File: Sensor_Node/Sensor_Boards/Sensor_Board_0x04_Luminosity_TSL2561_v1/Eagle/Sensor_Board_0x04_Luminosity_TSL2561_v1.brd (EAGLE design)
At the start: 55 x 35 mm, 16 parts, among them J1 M04_SMD_90, J4 ARDUINO_ISP, U2 ATMEGA328P_TQFP, Y1 8MHZ

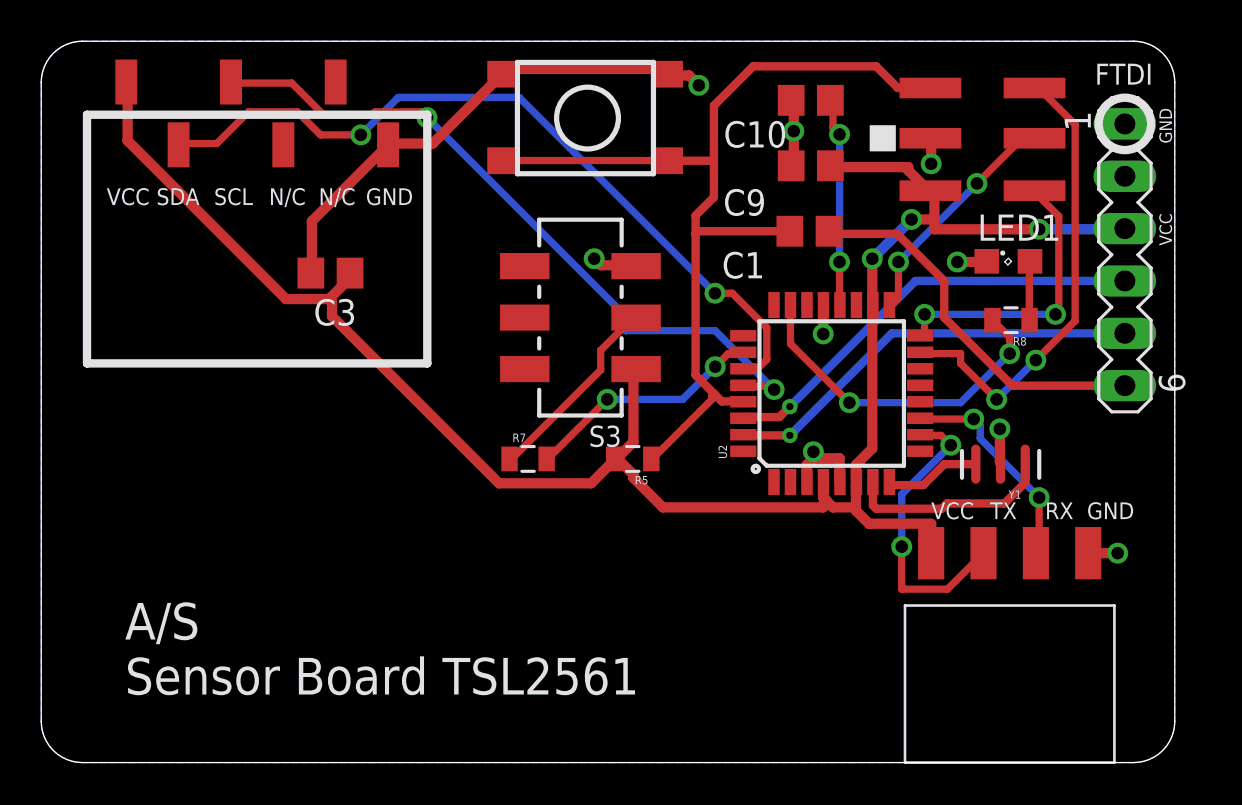
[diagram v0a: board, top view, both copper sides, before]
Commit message: Update SensorBoard TSL2561
new reference print - updated all placements, defined positions of
connectors and improved routing.
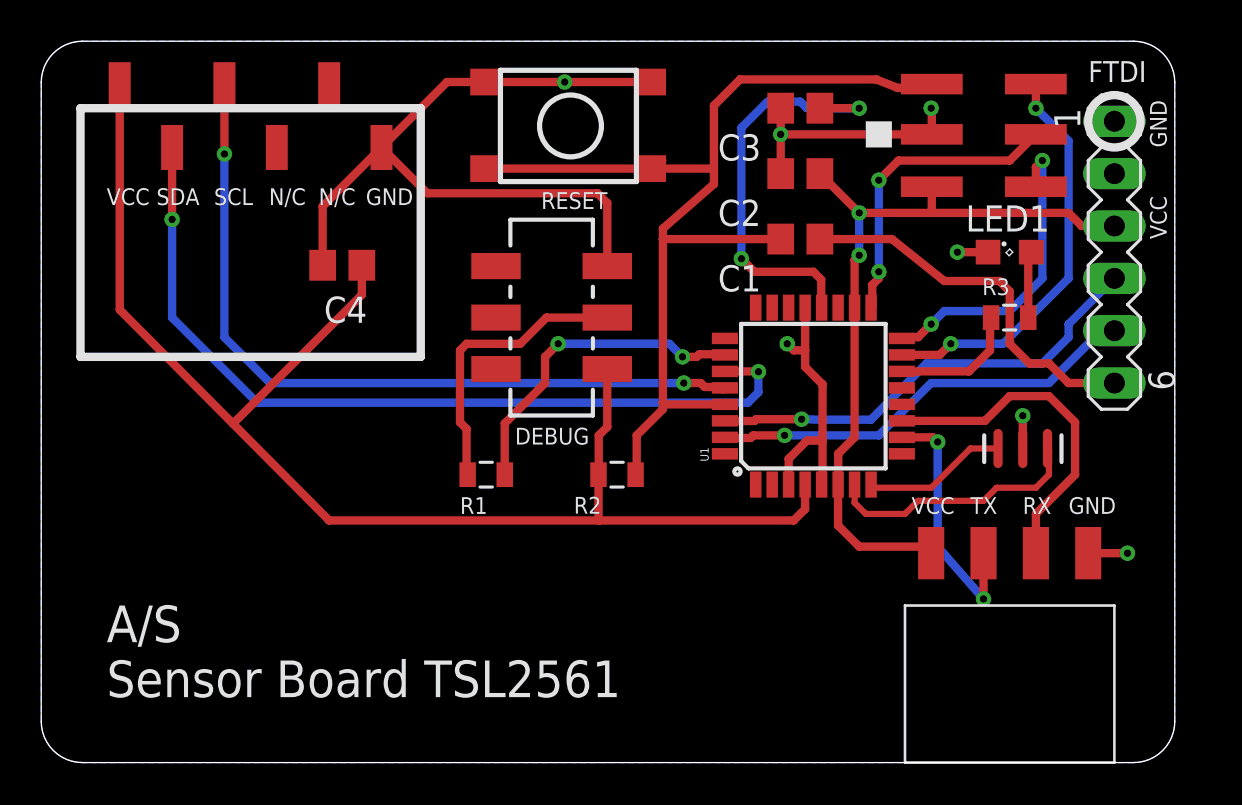
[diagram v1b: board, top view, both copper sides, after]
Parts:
- removed C10, C9: 100n, eagle-ltspice:C0805
- removed R5, R7: 10k, SparkFun-Passives:0805
- removed R8: 330, SparkFun-Passives:0805
- removed S3: JS202011SCQN, myownthings:JS202011SCQN
- removed U$9: M06_SMD_STRAIGHT, wsn:M06_SMD_STRAIGHT
- removed U2: ATMEGA328P_TQFP, marc_library:TQFP32-08
- added C2, C4: 100n, eagle-ltspice:C0805
- added R1, R2: 10k, SparkFun-Passives:0805
- added R3: 330, SparkFun-Passives:0805
- added S2: JS202011SCQN, myownthings:JS202011SCQN
- added SV2: (no value), con-lstb:MA06-1
- added U1: ATMEGA328P_TQFP, marc_library:TQFP32-08
- SV1: value (none) -> M06_SMD_STRAIGHT; device con-lstb:MA06-1 -> wsn:M06_SMD_STRAIGHT
- moved SV1 36.4 mm to (16.5, 29.8), turned to 180 degrees
- moved C3 24.2 mm to (36.8, 31.8)
- moved Y1 1.32 mm to (47.6, 15.2)
- moved S1 0.91 mm to (21.6, 33.0)
- moved C1 0.59 mm to (36.8, 25.4)
- moved LED1 0.45 mm to (47.0, 24.8)
- moved J4 0.20 mm to (48.3, 27.9)
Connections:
- net DBG_ENABLE: now also R1.2, U1.26; no longer R7.2, U2.26
- net FTDI_RESET: now also SV2.6; no longer SV1.6
- net FTDI_RXI: now also SV2.4, U1.30; no longer SV1.4, U2.30
- net FTDI_TXO: now also SV2.5, U1.31; no longer SV1.5, U2.31
- net GND: now also C2.2, C4.2, S2.3, SV1.P1, SV2.1, SV2.2, U1.21, U1.3, U1.5; no longer C10.2, C9.2, S3.3, SV1.1, SV1.2, U$9.P1, U2.21, U2.3, U2.5
- net L1: now also R3.2, U1.14; no longer R8.2, U2.23
- net MCU_RXI: now also U1.11; no longer U2.11
- net MCU_TXO: now also U1.10; no longer U2.10
- net MISO: now also U1.16; no longer U2.16
- net MOSI: now also U1.15; no longer U2.15
- net N$1: now also U1.8; no longer U2.8
- net N$15: now also C3.1, U1.20; no longer C10.1, U2.20
- net N$2: now also U1.7; no longer U2.7
- net N$3: now also R1.1, S2.2; no longer R7.1, S3.2
- net N$30: now also R3.1; no longer R8.1
- net RESET: now also R2.1, U1.29; no longer R5.1, U2.29
- net SCK: now also U1.17; no longer U2.17
- net SCL: now also SV1.P4, U1.28; no longer U$9.P4, U2.28
- net SDA: now also SV1.P5, U1.27; no longer U$9.P5, U2.27
- net VCC: now also C2.1, C4.1, R2.2, S2.1, SV1.P6, SV2.3, U1.18, U1.4, U1.6; no longer C3.1, C9.1, R5.2, S3.1, SV1.3, U$9.P6, U2.18, U2.4, U2.6
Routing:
- net GND: track 41.6 -> 66.4 mm, vias 9 -> 7
- net VCC: track 93.4 -> 104.9 mm, vias 3 -> 2
- net L1: track 16.7 -> 6.31 mm, vias 2 -> 0
- net N$15: track 10.1 -> 20.3 mm
- net MCU_RXI: track 10.7 -> 16.6 mm, vias 2 -> 0
- net N$3: track 9.53 -> 14.0 mm
- net DBG_ENABLE: track 11.7 -> 15.8 mm
- net RESET: track 47.4 -> 51.3 mm
- net SCK: track 11.4 -> 14.9 mm
- net SDA: track 37.9 -> 41.2 mm
- net MOSI: track 22.7 -> 19.7 mm
- net SCL: track 34.8 -> 37.7 mm
- net N$2: track 10.0 -> 12.6 mm
- net N$1: track 4.68 -> 7.01 mm
- net MCU_TXO: track 14.4 -> 12.5 mm
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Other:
- board text added: "DEBUG"
- board text added: "RESET"

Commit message: Finished Changes on PulseBoard
Pulseboard:
- tidied up routing and placement

TSL2561:
- tidied up some connections
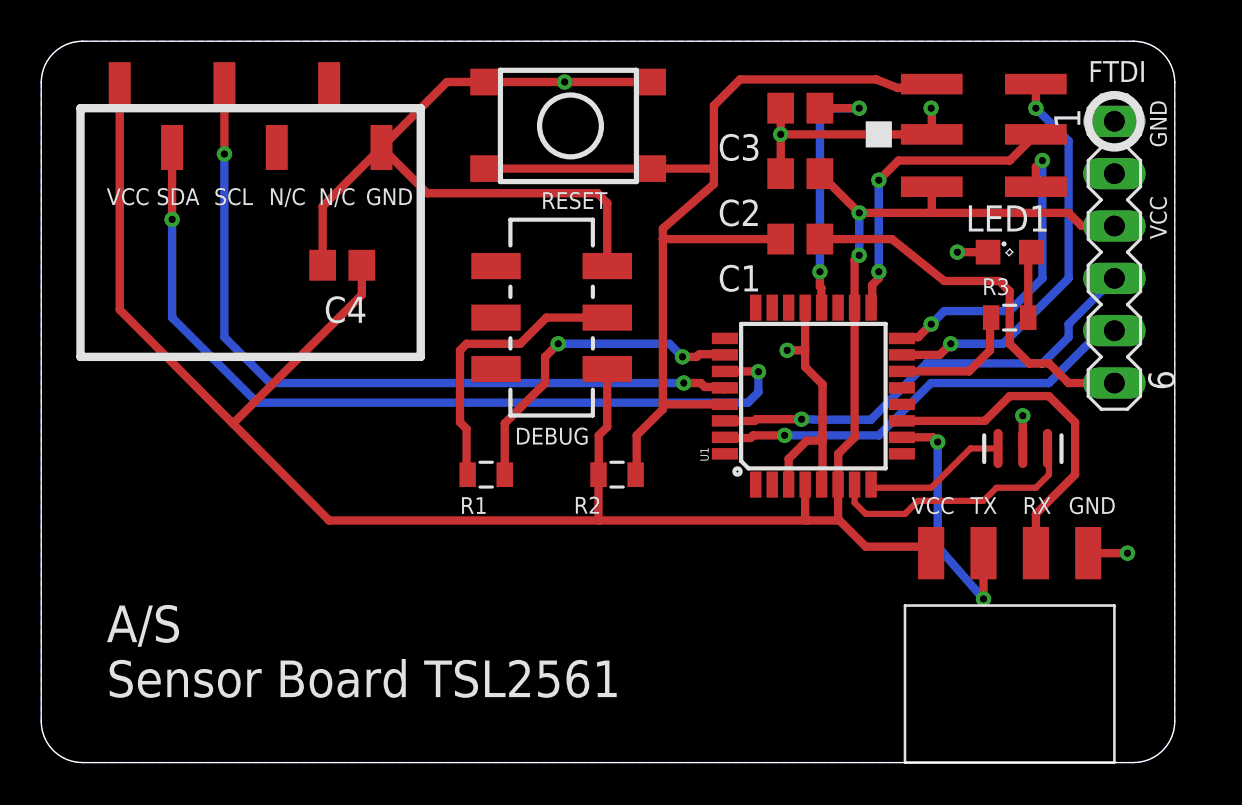
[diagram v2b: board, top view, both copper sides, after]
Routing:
- net N$15: track 20.3 -> 13.2 mm
- net VCC: track 104.9 -> 106.8 mm
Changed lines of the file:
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@@
 <?xml version="1.0" encoding="utf-8"?>
 <!DOCTYPE eagle SYSTEM "eagle.dtd">
-<eagle version="8.2.2">
+<eagle version="8.4.1">
 <drawing>
 <settings>
 <setting alwaysvectorfont="no"/>
+<setting keepoldvectorfont="yes"/>
 <setting verticaltext="up"/>
 </settings>
@@
 <param name="dpMaxLengthDifference" value="10mm"/>
 <param name="dpGapFactor" value="2.5"/>
-<param name="checkGrid" value="0"/>
 <param name="checkAngle" value="0"/>
 <param name="checkFont" value="1"/>
 <param name="checkRestrict" value="1"/>
+<param name="checkStop" value="0"/>
 <param name="useDiameter" value="13"/>
 <param name="maxErrors" value="50"/>
@@
 <wire x1="37.89541875" y1="15.621" x2="37.9095" y2="15.63508125" width="0.4064" layer="1"/>
 <via x="35.8775" y="30.48" extent="1-16" drill="0.35"/>
-<via x="36.195" y="20.32" extent="1-16" drill="0.35"/>
-<wire x1="37.065" y1="20.0025" x2="36.5125" y2="20.0025" width="0.4064" layer="1"/>
-<wire x1="36.5125" y1="20.0025" x2="36.195" y2="20.32" width="0.4064" layer="1"/>
+<via x="36.195" y="20.0025" extent="1-16" drill="0.35"/>
+<wire x1="37.065" y1="20.0025" x2="36.195" y2="20.0025" width="0.4064" layer="1"/>
 <via x="52.705" y="10.16" extent="1-16" drill="0.35"/>
 <wire x1="50.8" y1="10.16" x2="52.705" y2="10.16" width="0.4064" layer="1"/>
@@
 <wire x1="9.3053375" y1="16.441315625" x2="3.81" y2="21.971" width="0.4064" layer="1"/>
 <wire x1="9.3053375" y1="16.441315625" x2="13.97" y2="11.7475" width="0.4064" layer="1"/>
-<wire x1="37.065" y1="13.4874" x2="37.065" y2="12.3" width="0.4064" layer="1"/>
-<wire x1="37.065" y1="12.3" x2="36.5125" y2="11.7475" width="0.4064" layer="1"/>
-<wire x1="27.07931875" y1="11.7475" x2="36.5125" y2="11.7475" width="0.4064" layer="1"/>
-<wire x1="27.07931875" y1="11.7475" x2="13.97" y2="11.7475" width="0.4064" layer="1"/>
+<wire x1="13.97" y1="11.7475" x2="27.07931875" y2="11.7475" width="0.4064" layer="1"/>
 <wire x1="27.04" y1="13.97" x2="27.04" y2="11.78681875" width="0.4064" layer="1"/>
 <wire x1="27.04" y1="11.78681875" x2="27.07931875" y2="11.7475" width="0.4064" layer="1"/>
 <wire x1="15.555" y1="24.13" x2="15.555" y2="22.690978125" width="0.4064" layer="1"/>
 <wire x1="15.555" y1="22.690978125" x2="9.3053375" y2="16.441315625" width="0.4064" layer="1"/>
-<wire x1="38.665" y1="13.4874" x2="38.665" y2="11.5" width="0.4064" layer="1"/>
-<wire x1="38.665" y1="11.5" x2="39.6875" y2="10.4775" width="0.4064" layer="1"/>
-<wire x1="39.6875" y1="10.4775" x2="42.8625" y2="10.4775" width="0.4064" layer="1"/>
+<wire x1="38.665" y1="11.8175" x2="38.665" y2="13.4874" width="0.4064" layer="1"/>
+<wire x1="38.665" y1="11.7475" x2="38.665" y2="11.8175" width="0.4064" layer="1"/>
+<wire x1="38.665" y1="11.8175" x2="40.005" y2="10.4775" width="0.4064" layer="1"/>
+<wire x1="40.005" y1="10.4775" x2="42.8625" y2="10.4775" width="0.4064" layer="1"/>
 <wire x1="42.8625" y1="10.4775" x2="43.18" y2="10.16" width="0.4064" layer="1"/>
 <wire x1="39.465" y1="15.7795" x2="39.465" y2="22.0726" width="0.4064" layer="1"/>
@@
 <wire x1="49.8475" y1="26.67" x2="50.4825" y2="26.035" width="0.4064" layer="1"/>
 <wire x1="50.4825" y1="26.035" x2="52.07" y2="26.035" width="0.4064" layer="1"/>
-<wire x1="37.065" y1="13.4874" x2="38.6715" y2="13.4939" width="0" layer="19" extent="1-1"/>
+<wire x1="37.1475" y1="11.7475" x2="27.07931875" y2="11.7475" width="0.4064" layer="1"/>
+<wire x1="37.1475" y1="11.7475" x2="38.665" y2="11.7475" width="0.4064" layer="1"/>
+<wire x1="37.065" y1="11.83" x2="37.1475" y2="11.7475" width="0.4064" layer="1"/>
+<wire x1="37.065" y1="13.4874" x2="37.065" y2="11.83" width="0.4064" layer="1"/>
 </signal>
 <signal name="RESET">
@@
 <contactref element="C3" pad="1"/>
 <contactref element="U1" pad="20"/>
+<wire x1="37.78" y1="31.75" x2="39.6875" y2="31.75" width="0.4064" layer="1"/>
 <via x="39.6875" y="31.75" extent="1-16" drill="0.35"/>
-<wire x1="37.78" y1="31.75" x2="39.6875" y2="31.75" width="0.4064" layer="1"/>
-<wire x1="39.6875" y1="31.75" x2="37.1475" y2="31.75" width="0.4064" layer="16"/>
-<wire x1="37.1475" y1="31.75" x2="36.83" y2="32.0675" width="0.4064" layer="16"/>
-<wire x1="36.83" y1="32.0675" x2="35.2425" y2="32.0675" width="0.4064" layer="16"/>
-<wire x1="35.2425" y1="32.0675" x2="33.9725" y2="30.7975" width="0.4064" layer="16"/>
-<wire x1="33.9725" y1="30.7975" x2="33.9725" y2="24.4475" width="0.4064" layer="16"/>
-<via x="33.9725" y="24.4475" extent="1-16" drill="0.35"/>
-<wire x1="33.9725" y1="24.4475" x2="34.6075" y2="23.8125" width="0.4064" layer="1"/>
-<wire x1="34.6075" y1="23.8125" x2="37.465" y2="23.8125" width="0.4064" layer="1"/>
-<wire x1="37.465" y1="23.8125" x2="37.846" y2="23.4315" width="0.4064" layer="1"/>
-<wire x1="37.846" y1="23.4315" x2="37.846" y2="22.0916" width="0.4064" layer="1"/>
-<wire x1="37.846" y1="22.0916" x2="37.865" y2="22.0726" width="0.4064" layer="1"/>
+<wire x1="39.6875" y1="31.75" x2="38.4175" y2="31.75" width="0.4064" layer="16"/>
+<wire x1="38.4175" y1="31.75" x2="37.7825" y2="31.115" width="0.4064" layer="16"/>
+<wire x1="37.7825" y1="31.115" x2="37.7825" y2="23.8125" width="0.4064" layer="16"/>
+<via x="37.7825" y="23.8125" extent="1-16" drill="0.35"/>
+<wire x1="37.7825" y1="23.8125" x2="37.7825" y2="23.08821875" width="0.4064" layer="1"/>
+<wire x1="37.7825" y1="23.08821875" x2="37.85275625" y2="23.0179625" width="0.4064" layer="1"/>
+<wire x1="37.85275625" y1="23.0179625" x2="37.85275625" y2="22.08484375" width="0.4064" layer="1"/>
+<wire x1="37.85275625" y1="22.08484375" x2="37.865" y2="22.0726" width="0.4064" layer="1"/>
 </signal>
 <signal name="N$3">
@@
 </note>
 <note version="8.2" severity="warning">
-Since Version 8.2, Eagle supports online libraries. The ids
+Since Version 8.2, EAGLE supports online libraries. The ids
 of those online libraries will not be understood (or retained)
 with this version.

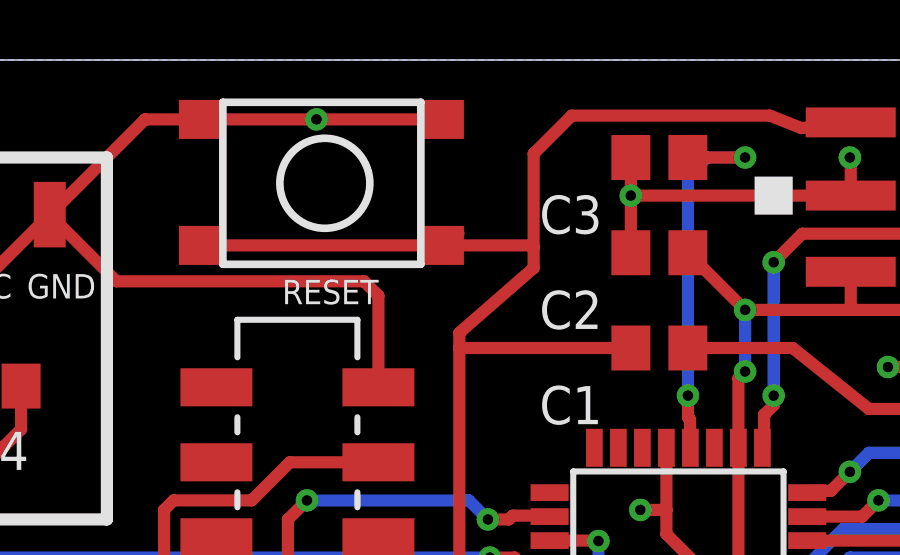
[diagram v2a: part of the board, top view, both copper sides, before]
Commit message: Started tidying of SHT31
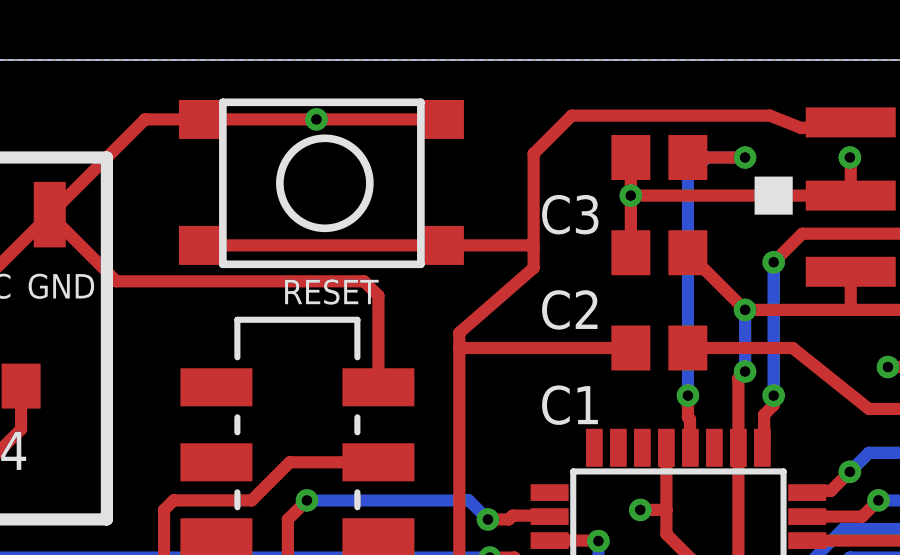
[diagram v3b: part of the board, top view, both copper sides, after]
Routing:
- net RESET: track 51.3 -> 50.6 mm
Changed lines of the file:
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@@
 <wire x1="33.9078" y1="33.1458" x2="32.639" y2="31.877" width="0.4064" layer="1"/>
 <wire x1="35.88" y1="25.4" x2="30.1625" y2="25.4" width="0.4064" layer="1"/>
-<wire x1="30.1625" y1="29.21" x2="29.54" y2="28.82" width="0.3556" layer="1"/>
 <wire x1="21.59" y1="28.82" x2="29.54" y2="28.82" width="0.4064" layer="1"/>
 <wire x1="29.54" y1="28.82" x2="32.568796875" y2="28.82" width="0.4064" layer="1"/>

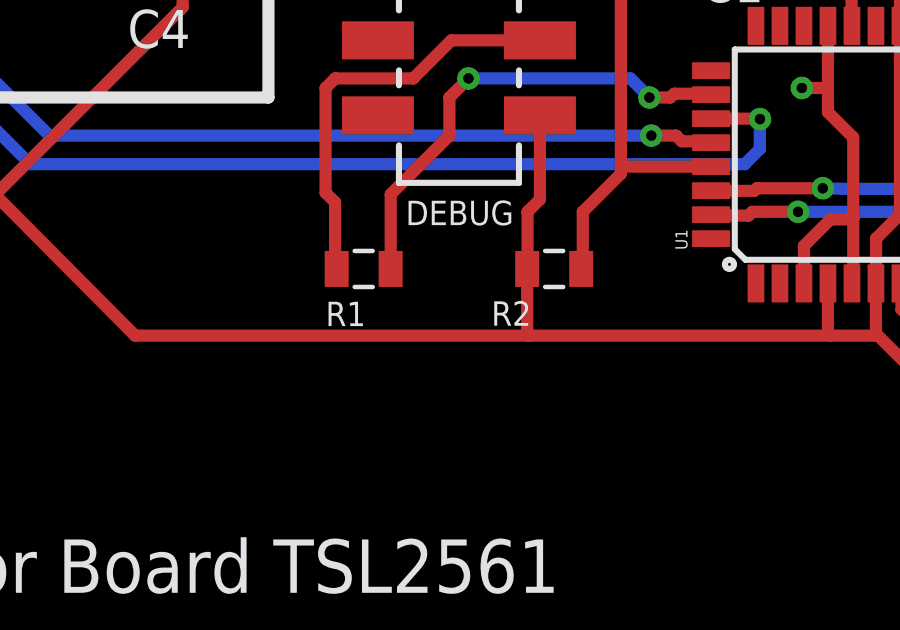
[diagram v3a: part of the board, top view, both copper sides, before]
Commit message: Finished SHT31 and CO2-Board
- finished tidying SHT31
- added FTDI-connector to CO2-Sensorboard
- tidied CO2-Sensorboard
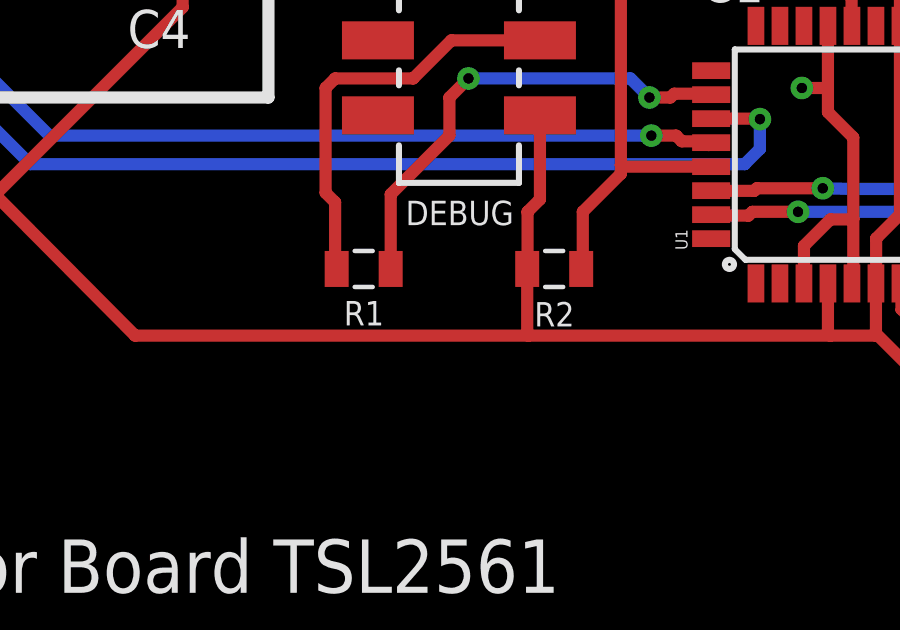
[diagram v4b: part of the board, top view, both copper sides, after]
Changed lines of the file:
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@@
 <?xml version="1.0" encoding="utf-8"?>
 <!DOCTYPE eagle SYSTEM "eagle.dtd">
-<eagle version="8.4.1">
+<eagle version="8.4.2">
 <drawing>
 <settings>
@@
 </element>
 <element name="R2" library="SparkFun-Passives" package="0805" value="10k" x="27.94" y="13.97" smashed="yes" rot="R180">
-<attribute name="NAME" x="27.178" y="12.8905" size="0.8128" layer="21" rot="R180"/>
+<attribute name="NAME" x="28.61355625" y="12.866165625" size="0.8128" layer="21" rot="R180"/>
 </element>
 <element name="R1" library="SparkFun-Passives" package="0805" value="10k" x="21.59" y="13.97" smashed="yes">
-<attribute name="NAME" x="20.32" y="12.065" size="0.8128" layer="21"/>
+<attribute name="NAME" x="20.928284375" y="12.089334375" size="0.8128" layer="21"/>
 </element>
 <element name="R3" library="SparkFun-Passives" package="0805" value="330" x="46.99" y="21.59" smashed="yes" rot="R180">
